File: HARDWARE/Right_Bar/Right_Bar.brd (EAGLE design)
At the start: 88.9 x 39.4 mm, 13 parts, among them J1 TRRS

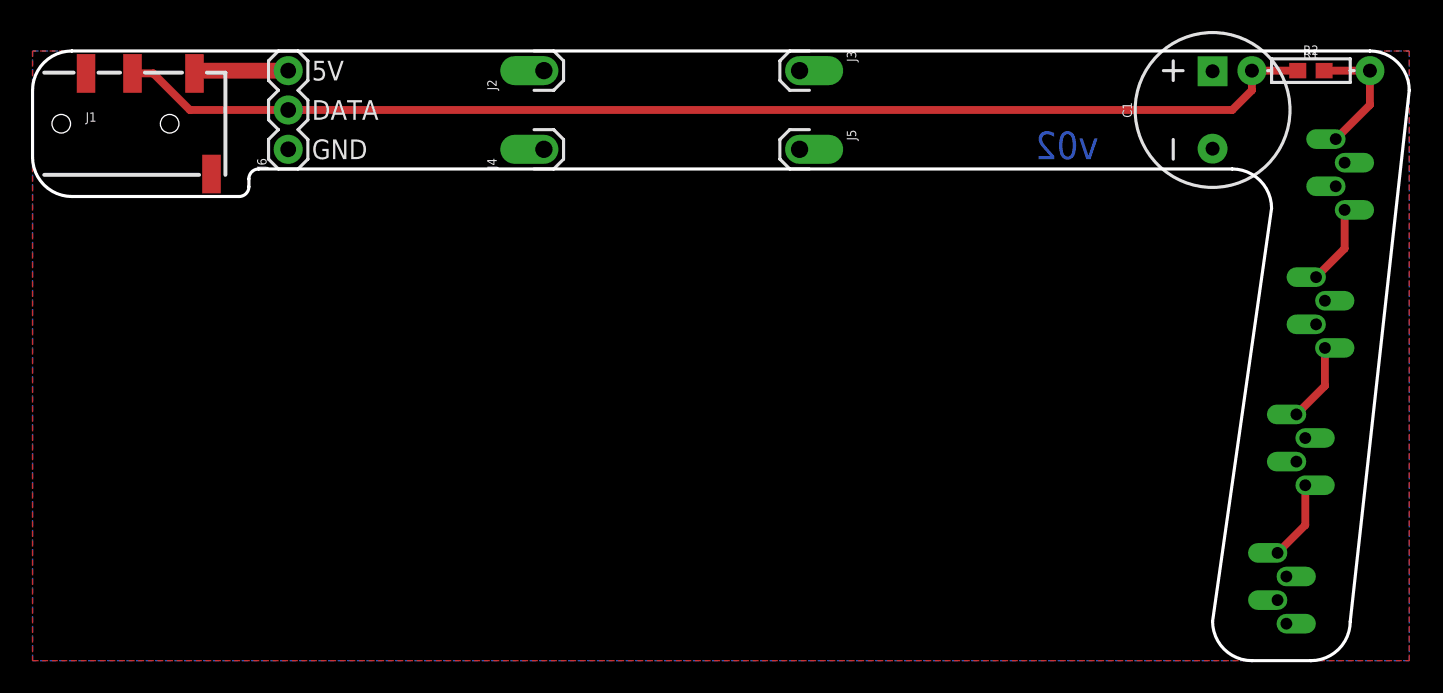
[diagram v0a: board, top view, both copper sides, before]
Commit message: renames right and left, finished left
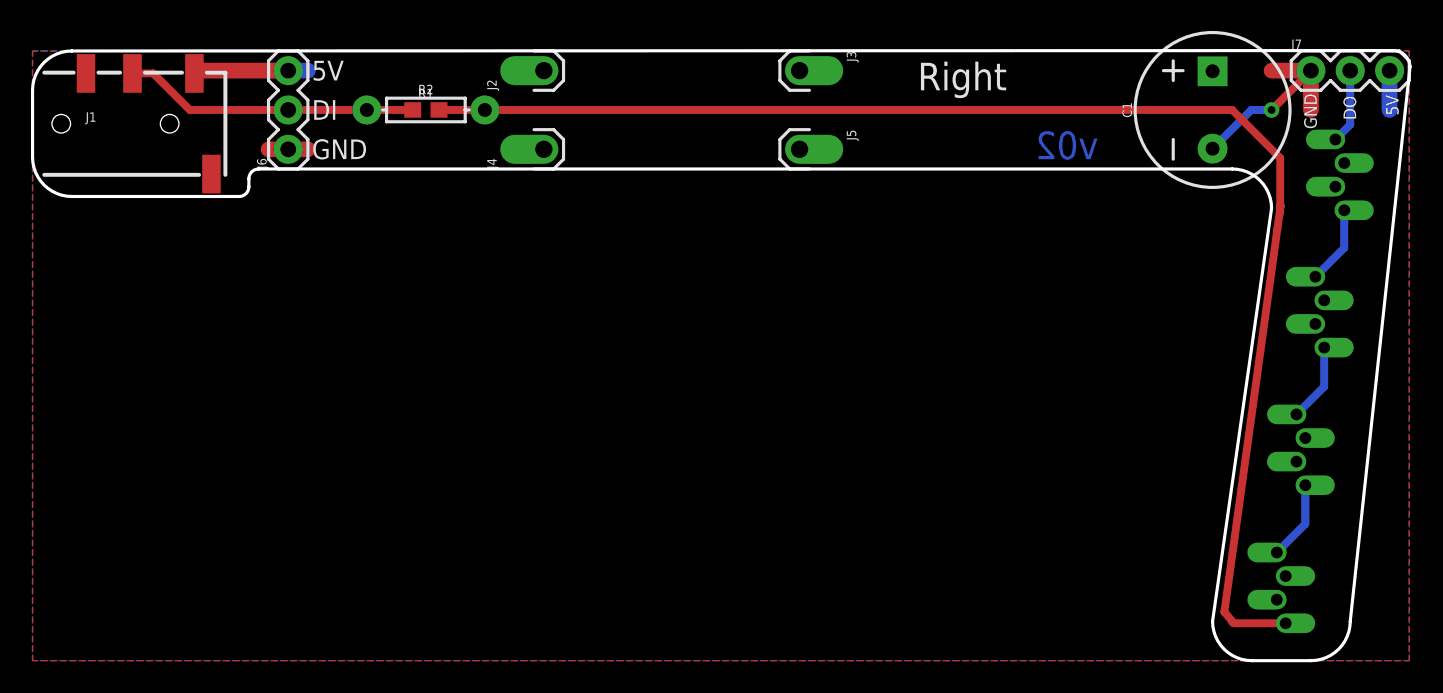
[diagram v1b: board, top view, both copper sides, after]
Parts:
- added J7: (no value), SparkFun-Connectors:1X03
- moved R1 57.2 mm to (25.4, 35.6)
- moved R2 57.2 mm to (25.4, 35.6)
- moved U$4 27.3 mm to (84.8, 31.5), turned to 270 degrees
- moved U$3 26.6 mm to (81.0, 4.83), turned to 270 degrees
- moved U$1 9.35 mm to (83.5, 22.6), turned to 270 degrees
- moved U$2 8.63 mm to (82.3, 13.7), turned to 270 degrees
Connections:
- net DATA renamed DI
- new net DO: J7.2, U$4.4
- net 5V: now also J7.3
- net GND: now also J7.1
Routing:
- net N$2: track 8.29 -> 89.5 mm
- net DI: track 78.0 -> 19.1 mm
- net GND: track 0.00 -> 16.1 mm, vias 0 -> 2
- net 5V: track 6.24 -> 11.3 mm
- net DO: track 0.00 -> 4.84 mm
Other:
- board size 88.9 x 39.4 mm -> 89 x 39.4 mm
- board text added: "DI"
- board text added: "DO"
- board text added: "Right"
- board text removed: "DATA"
